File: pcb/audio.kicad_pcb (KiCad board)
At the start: 2 copper layers, 19 x 57.4 mm, 5 parts, among them SW1 SW_Push, SW2 SW_Push, SW3 SW_Push, U1 MOUDLE-SEEEDUINO-XIAO

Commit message: Widen the PCB outline to 22 mm and update the case model.
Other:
- board size 19 x 57.4 mm -> 22 x 57.4 mm
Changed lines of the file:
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@@
 	)
 	(gr_rect
-		(start 57.5 43.5)
-		(end 76.5 100.9)
+		(start 56 43.5)
+		(end 78 100.9)
 		(stroke
 			(width 0.05)

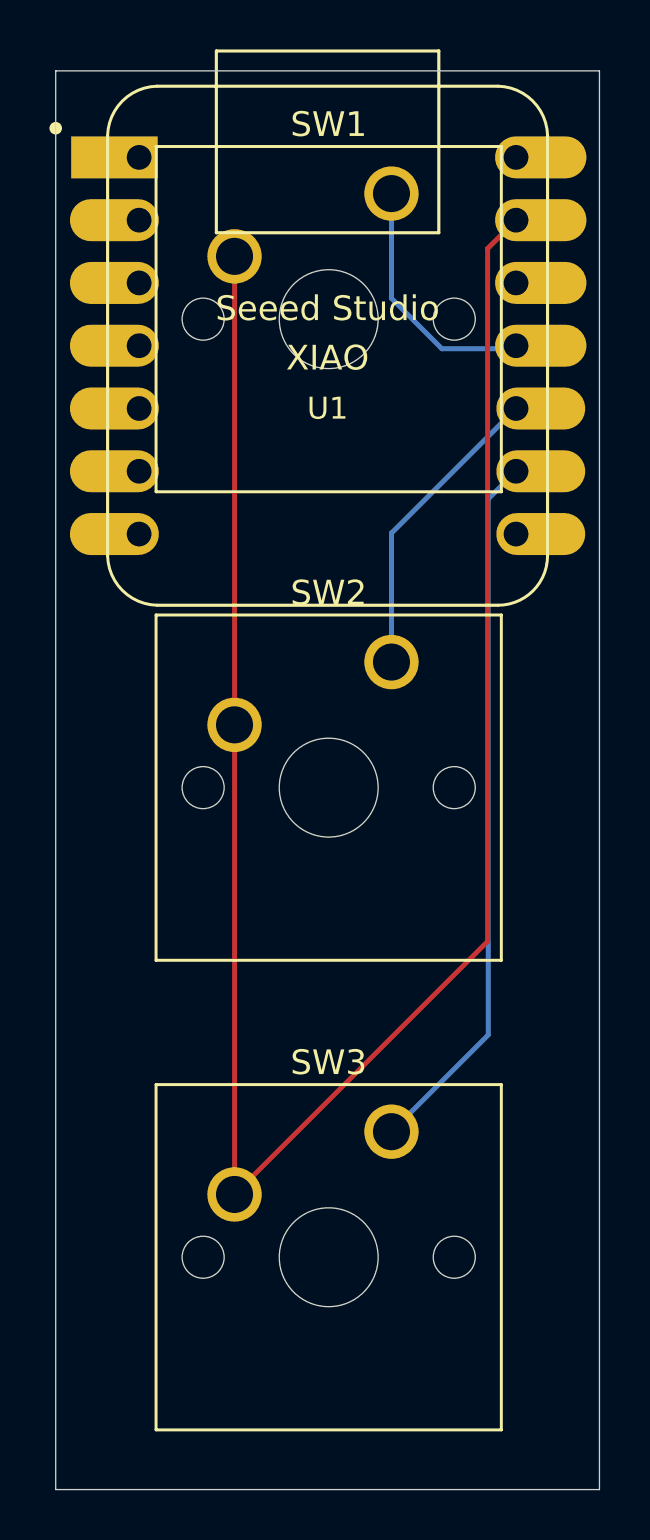
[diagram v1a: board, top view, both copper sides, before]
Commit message: Add the final 3D models and make the PCB model paths relative.
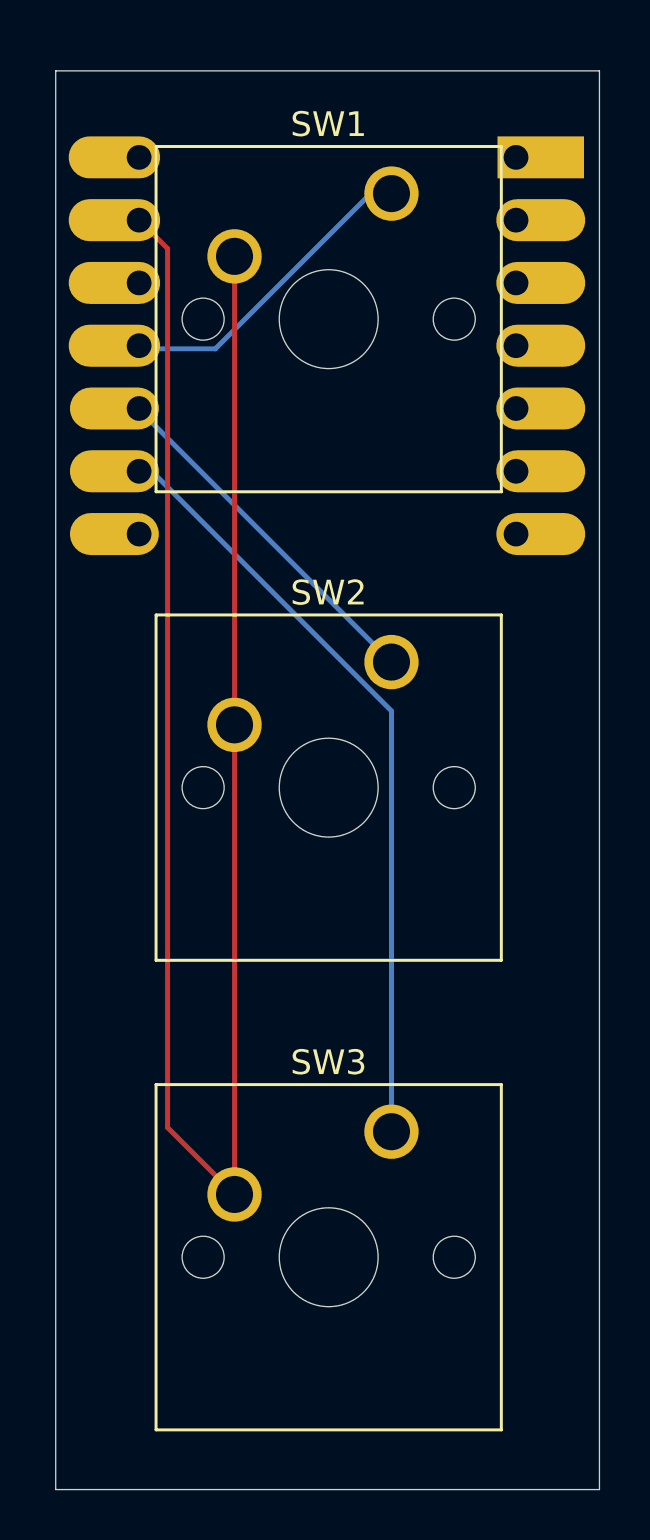
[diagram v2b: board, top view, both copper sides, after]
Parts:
- U1: moved to B.Cu
- turned U1 to 180 degrees
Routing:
- net GND: track 82.1 -> 79.3 mm
- net Net-(U1-PA6_A10_D10_MOSI): track 10.2 -> 12.9 mm
- net Net-(U1-PA7_A8_D8_SCK): track 28.8 -> 31.2 mm
- net Net-(U1-PA5_A9_D9_MISO): track 12.3 -> 14.5 mm
